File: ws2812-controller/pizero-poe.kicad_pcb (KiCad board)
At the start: 2 copper layers, 81.8 x 30 mm, 70 parts, among them IC1 ENC28J60-I/ML, J1 RJ45-LED, P1 Raspberry_Pi_+_Conn, P2 WS2812 Cn., P3 WS2812 Cn., Q1 SI3440DV, Q2 BSS138, Q3 BSS138, T1 PULSE_H1197, T2 TRANSFO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

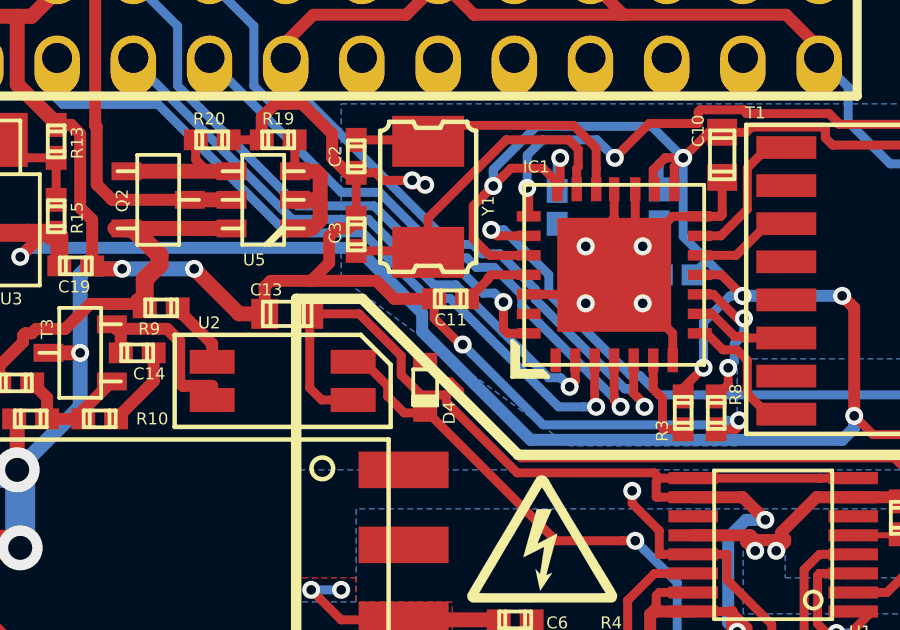
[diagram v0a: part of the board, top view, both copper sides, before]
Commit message: changed cap size, wrong value
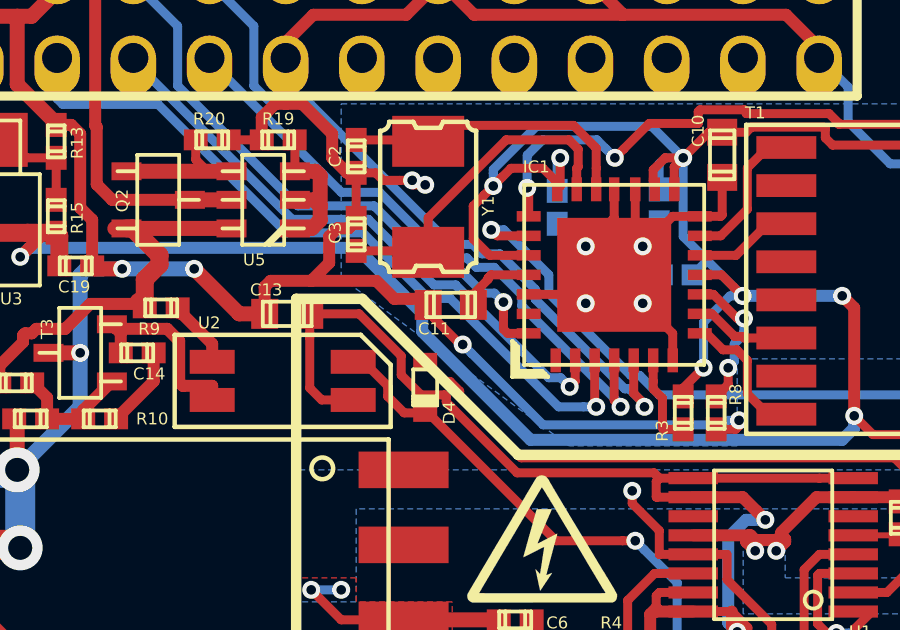
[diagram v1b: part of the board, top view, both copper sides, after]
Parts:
- C11: footprint w_smd_cap:c_0402 -> w_smd_cap:c_0603
- C2, C3: value C -> 16pf
- R25: value R -> 100
- moved C11 0.20 mm to (150.5, 90.9)
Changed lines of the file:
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@@
   (general
     (links 167)
-    (no_connects 2)
-    (area 129.349999 77.012809 211.250001 107.112811)
+    (no_connects 4)
+    (area 106.149999 77.812809 188.050001 107.912811)
     (thickness 1.6)
     (drawings 35)
@@
       (effects (font (size 0.4 0.4) (thickness 0.125)))
     )
-    (fp_text value C (at 0 0.4826 270) (layer F.SilkS) hide
+    (fp_text value 16pf (at 0 0.4826 270) (layer F.SilkS) hide
       (effects (font (size 0.4 0.4) (thickness 0.125)))
     )
@@
       (effects (font (size 0.4 0.4) (thickness 0.125)))
     )
-    (fp_text value C (at 0 0.4826 90) (layer F.SilkS) hide
+    (fp_text value 16pf (at 0 0.4826 90) (layer F.SilkS) hide
       (effects (font (size 0.4 0.4) (thickness 0.125)))
     )
@@
       (net 1 GND))
     (model walter/smd_cap/c_0603.wrl
-      (at (xyz 0 0 0))
-      (scale (xyz 1 1 1))
-      (rotate (xyz 0 0 0))
-    )
-  )
-  (module w_smd_cap:c_0402 (layer F.Cu)
-    (at 150.44864 90.7 180)
-    (descr "SMT capacitor, 0402")
-    (fp_text reference C11 (at 0 -0.7 180) (layer F.SilkS)
-      (effects (font (size 0.4 0.4) (thickness 0.125)))
-    )
-    (fp_text value C (at 0 0.4826 180) (layer F.SilkS) hide
-      (effects (font (size 0.4 0.4) (thickness 0.125)))
-    )
-    (fp_line (start 0.3302 -0.2794) (end 0.3302 0.2794) (layer F.SilkS) (width 0.127))
-    (fp_line (start -0.3302 -0.2794) (end -0.3302 0.2794) (layer F.SilkS) (width 0.127))
-    (fp_line (start -0.5334 -0.2794) (end -0.5334 0.2794) (layer F.SilkS) (width 0.127))
-    (fp_line (start -0.5334 0.2794) (end 0.5334 0.2794) (layer F.SilkS) (width 0.127))
-    (fp_line (start 0.5334 0.2794) (end 0.5334 -0.2794) (layer F.SilkS) (width 0.127))
-    (fp_line (start 0.5334 -0.2794) (end -0.5334 -0.2794) (layer F.SilkS) (width 0.127))
-    (pad 1 smd rect (at 0.54864 0 180) (size 0.8001 0.6985) (layers F.Cu F.Paste F.Mask)
-      (net 1 GND))
-    (pad 2 smd rect (at -0.54864 0 180) (size 0.8001 0.6985) (layers F.Cu F.Paste F.Mask)
-      (net 11 "Net-(C11-Pad2)"))
-    (model walter/smd_cap/c_0402.wrl
       (at (xyz 0 0 0))
       (scale (xyz 1 1 1))
@@
       (effects (font (size 0.4 0.4) (thickness 0.125)))
     )
-    (fp_text value R (at 0 -0.4826 180) (layer B.SilkS) hide
+    (fp_text value 100 (at 0 -0.4826 180) (layer B.SilkS) hide
       (effects (font (size 0.4 0.4) (thickness 0.125)))
     )
@@
       (xy 0.50546 -0.1778) (xy 0.508 -0.1778) (xy 0.508 -0.1778)) (layer F.SilkS) (width 0.00254))
   )
+  (module w_smd_cap:c_0603 (layer F.Cu)
+    (at 150.45184 90.9 180)
+    (descr "SMT capacitor, 0603")
+    (fp_text reference C11 (at 0.55184 -0.8 180) (layer F.SilkS)
+      (effects (font (size 0.4 0.4) (thickness 0.1)))
+    )
+    (fp_text value C (at 0 0.635 180) (layer F.SilkS) hide
+      (effects (font (size 0.20066 0.20066) (thickness 0.04064)))
+    )
+    (fp_line (start 0.5588 0.4064) (end 0.5588 -0.4064) (layer F.SilkS) (width 0.127))
+    (fp_line (start -0.5588 -0.381) (end -0.5588 0.4064) (layer F.SilkS) (width 0.127))
+    (fp_line (start -0.8128 -0.4064) (end 0.8128 -0.4064) (layer F.SilkS) (width 0.127))
+    (fp_line (start 0.8128 -0.4064) (end 0.8128 0.4064) (layer F.SilkS) (width 0.127))
+    (fp_line (start 0.8128 0.4064) (end -0.8128 0.4064) (layer F.SilkS) (width 0.127))
+    (fp_line (start -0.8128 0.4064) (end -0.8128 -0.4064) (layer F.SilkS) (width 0.127))
+    (pad 1 smd rect (at 0.75184 0 180) (size 0.89916 1.00076) (layers F.Cu F.Paste F.Mask)
+      (net 1 GND))
+    (pad 2 smd rect (at -0.75184 0 180) (size 0.89916 1.00076) (layers F.Cu F.Paste F.Mask)
+      (net 11 "Net-(C11-Pad2)"))
+    (model walter/smd_cap/c_0603.wrl
+      (at (xyz 0 0 0))
+      (scale (xyz 1 1 1))
+      (rotate (xyz 0 0 0))
+    )
+  )
   (gr_text "To Do:\n- check all diodes to see if they are reversed\n- create labeling for PoEPi\n- check schematic and PoE ciruit for errors\n" (at 76.4 135.7) (layer F.Fab)

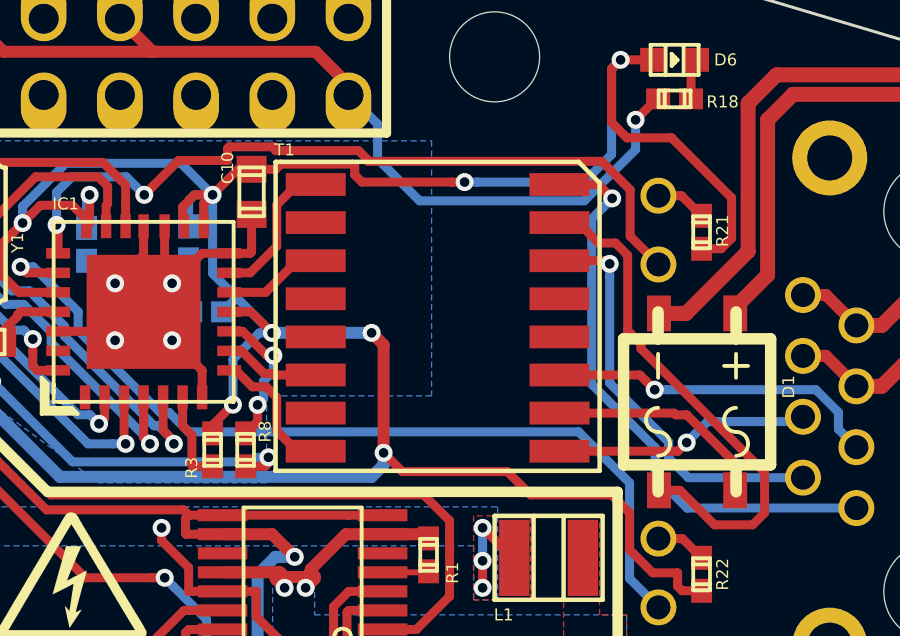
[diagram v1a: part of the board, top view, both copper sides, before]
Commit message: added EMI components after update
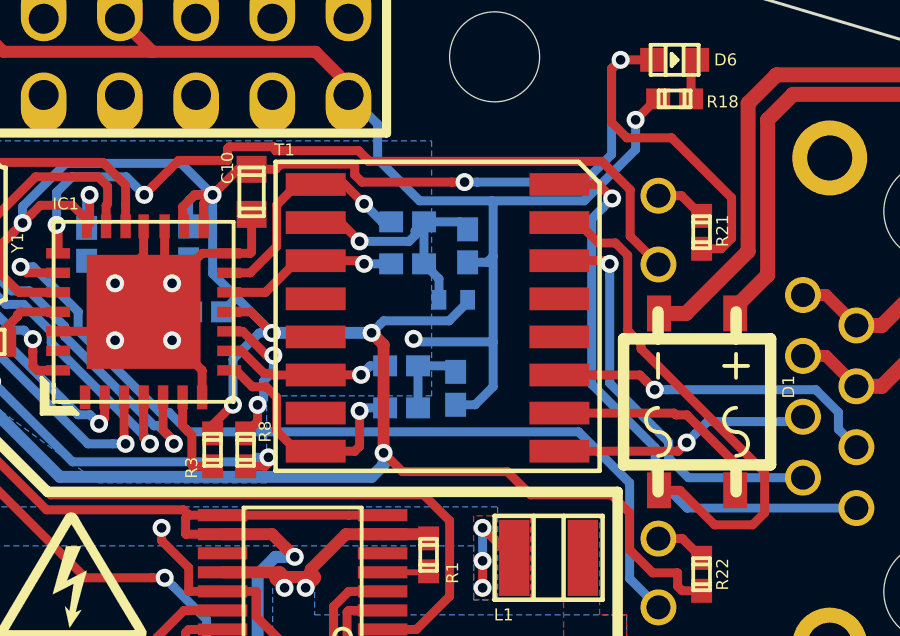
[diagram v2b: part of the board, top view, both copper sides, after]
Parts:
- added C18: 0.1uf, w_smd_cap:c_0402, B.Cu at (166.7, 87.7)
- added C21: 0.1uf, w_smd_cap:c_0402, B.Cu at (166.3, 92.4)
- added L2: BEAD, w_smd_inductors:inductor_smd_0402, B.Cu at (166.2, 89.5)
- added R14: 49.9, w_smd_resistors:r_0402, B.Cu at (164.7, 86.9)
- added R16: 49.9, w_smd_resistors:r_0402, B.Cu at (164.7, 88.3)
- added R17: 49.9, w_smd_resistors:r_0402, B.Cu at (164.5, 91.7)
- added R26: 49.9, w_smd_resistors:r_0402, B.Cu at (164.5, 93.1)
- C11: value C -> 10uf
- R3: value R -> 1k
- R8: value R -> 2.32k
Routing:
- net GND: track 216.6 -> 227.9 mm, vias 15 -> 16
- net Net-(C18-Pad2): track 0.00 -> 8.59 mm, vias 0 -> 1
- net +3V3: track 145.9 -> 149.6 mm
- net /TPIN-: track 4.03 -> 7.64 mm, vias 0 -> 1
- net /TPOUT+: track 4.29 -> 7.32 mm, vias 0 -> 1
- net Net-(C21-Pad1): track 0.00 -> 2.73 mm
- net /TPOUT-: track 2.70 -> 5.26 mm, vias 0 -> 1
- net /TPIN+: track 3.22 -> 5.66 mm, vias 0 -> 1

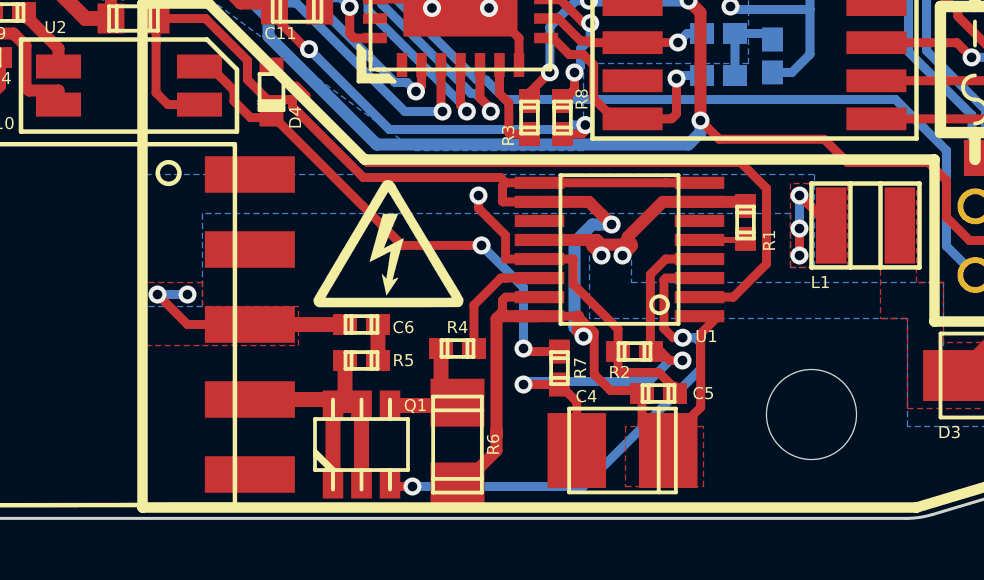
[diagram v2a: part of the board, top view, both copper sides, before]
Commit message: changed caps after reviewing notes
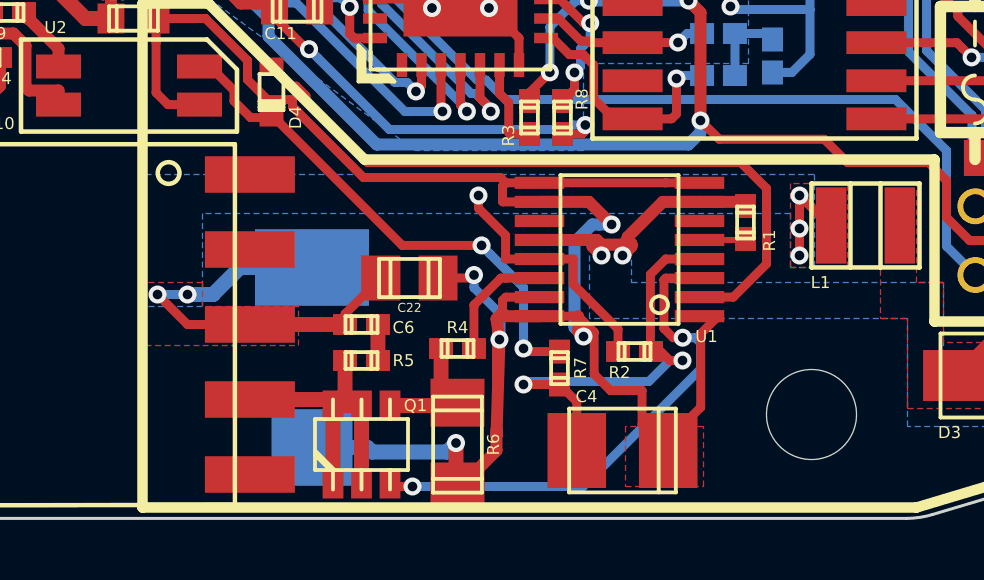
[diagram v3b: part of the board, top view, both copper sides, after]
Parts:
- removed G***: LOGO, w_logo:Logo_silk_high_voltage_5x4.2mm
- added C22: 1uf, w_smd_cap:c_0805, F.Cu at (154.2, 99.8)
- C4: value CP -> 220uf
- C5: value C -> 6.8uf; footprint w_smd_cap:c_0402 -> w_smd_cap:c_tant_D; moved to B.Cu
- R21, R22: value R -> 549
- moved C5 11.6 mm to (150.9, 102.5), turned to 270 degrees
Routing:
- net GNDPWR: track 62.5 -> 72.7 mm, vias 2 -> 5
- net Net-(C22-Pad1): track 22.7 -> 26.2 mm
- added copper zone on F.Cu, net Net-(C5-Pad1)
